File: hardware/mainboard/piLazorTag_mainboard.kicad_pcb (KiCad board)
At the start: 2 copper layers, 10 parts, among them M1 LOGIC_LEVEL_CONVERTER

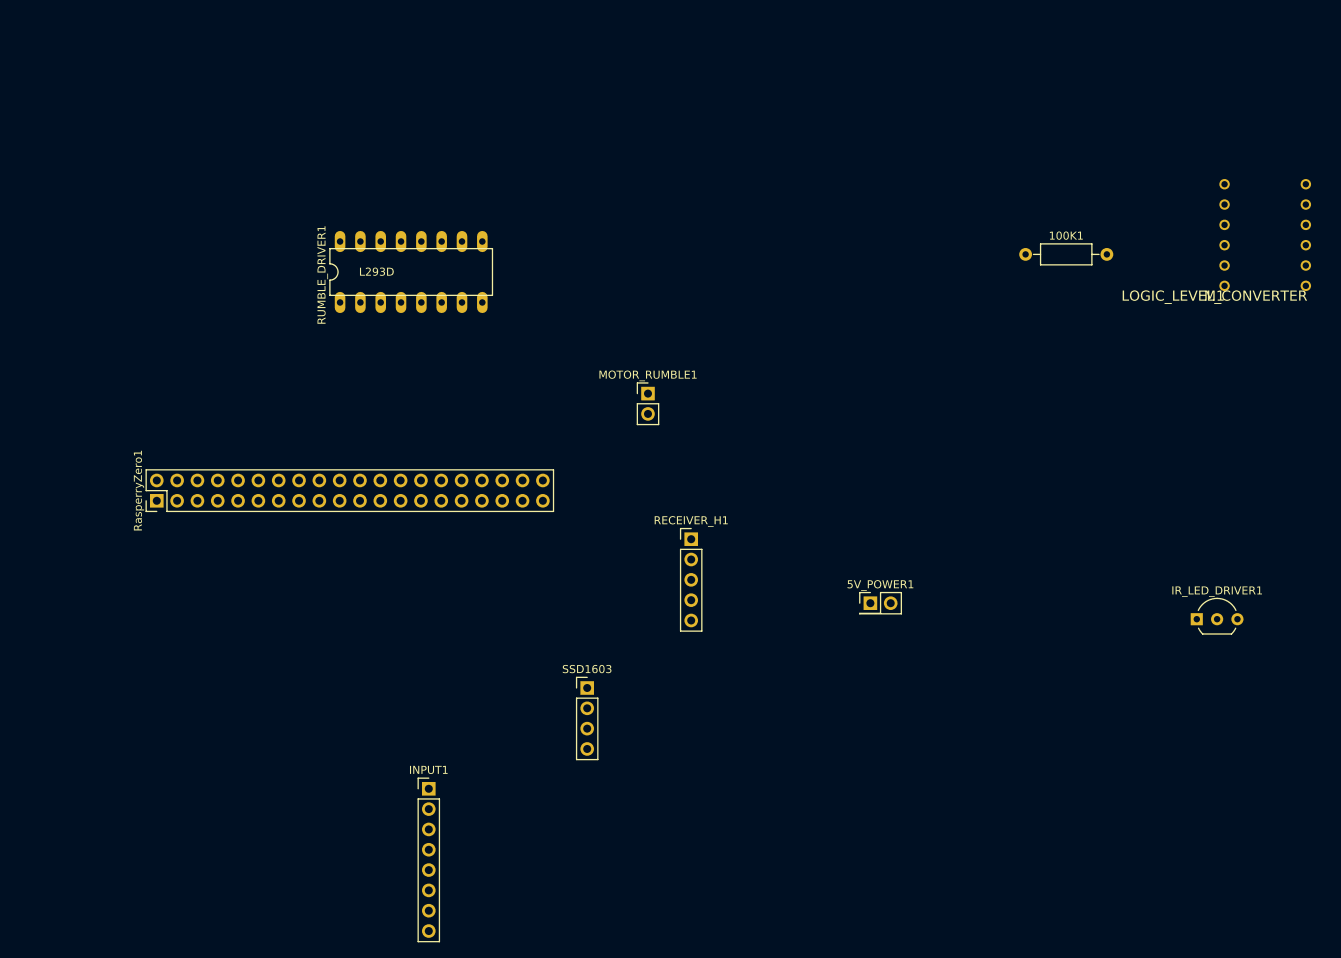
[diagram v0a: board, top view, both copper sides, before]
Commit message: #9 Reasigned some pins to get a better board layout
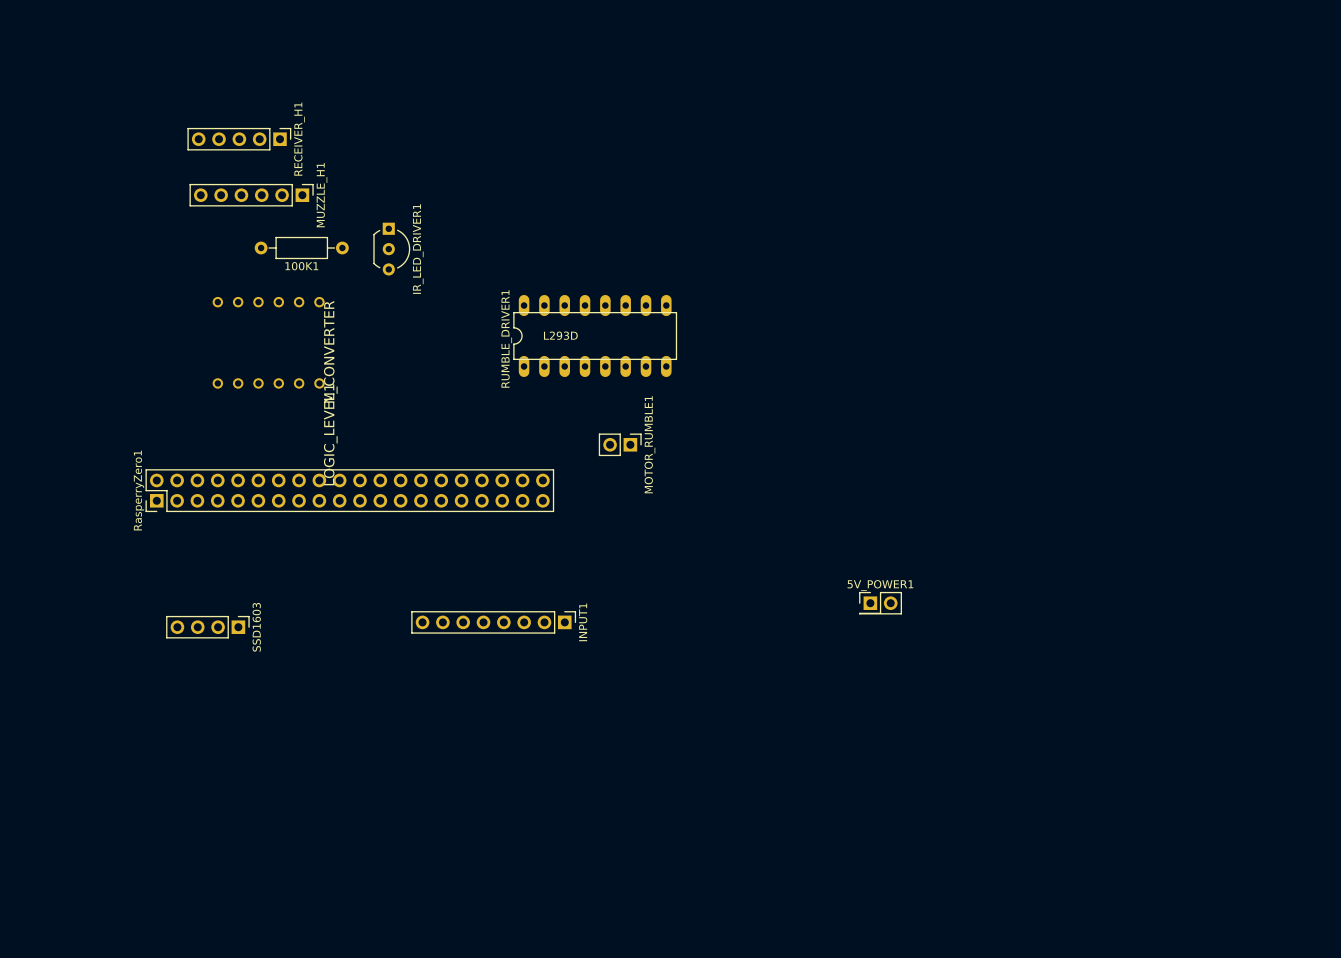
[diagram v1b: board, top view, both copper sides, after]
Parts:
- added MUZZLE_H1: CONN_01X06, Pin_Headers:Pin_Header_Straight_1x06_Pitch2.54mm, F.Cu at (118.0, 74.8)
- moved IR_LED_DRIVER1 112.2 mm to (128.8, 79.0), turned to 270 degrees
- moved M1 111.3 mm to (121.4, 99.6), turned to 90 degrees
- moved 100K1 85.4 mm to (123.0, 81.4), turned to 180 degrees
- moved RECEIVER_H1 71.7 mm to (115.2, 67.8), turned to 270 degrees
- moved SSD1603 44.3 mm to (110.0, 128.8), turned to 270 degrees
- moved INPUT1 26.9 mm to (150.8, 128.2), turned to 270 degrees
- moved RUMBLE_DRIVER1 24.4 mm to (154.6, 92.4)
- moved MOTOR_RUMBLE1 6.77 mm to (159.0, 106.0), turned to 270 degrees
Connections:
- INPUT1 pad 3: Net-(INPUT1-Pad3) -> /G26
- INPUT1 pad 4: Net-(INPUT1-Pad4) -> /G19
- INPUT1 pad 5: Net-(INPUT1-Pad5) -> /G13
- INPUT1 pad 6: Net-(INPUT1-Pad6) -> /G6
- INPUT1 pad 7: Net-(INPUT1-Pad7) -> /G5
- INPUT1 pad 8: Net-(INPUT1-Pad8) -> /G22
- M1 pad P$1: Net-(M1-PadP$1) -> /G18
- M1 pad P$12: Net-(M1-PadP$12) -> /M_LED_DI
- M1 pad P$5: Net-(M1-PadP$5) -> /G23
- M1 pad P$6: Net-(M1-PadP$6) -> /G24
- M1 pad P$7: Net-(M1-PadP$7) -> Net-(100K1-Pad1)
- M1 pad P$8: Net-(M1-PadP$8) -> /IR_SIG
- RUMBLE_DRIVER1 pad 2: /PI_RUMBLE -> /G21

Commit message: #9 Further Progress on the mainboard
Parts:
- moved 5V_POWER1 25.2 mm to (163.8, 125.2), turned to 270 degrees
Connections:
- INPUT1 pad 8: /G22 -> /G11/spi
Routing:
- net +3V3: track 0.00 -> 96.2 mm
- net +5V: track 0.00 -> 29.1 mm
- net /G11/spi: track 0.00 -> 17.6 mm
- net /G3/i2c: track 0.00 -> 15.8 mm
- net /G2/i2c: track 0.00 -> 15.8 mm
- net /G19: track 0.00 -> 15.3 mm
- net /G6: track 0.00 -> 15.3 mm
- net /G5: track 0.00 -> 15.3 mm
- net /G26: track 0.00 -> 15.3 mm
- net /G13: track 0.00 -> 15.3 mm
- net /G21: track 0.00 -> 14.3 mm
- net /G18: track 0.00 -> 14.2 mm
- net Net-(MOTOR_RUMBLE1-Pad2): track 0.00 -> 12.1 mm
- net /G23: track 0.00 -> 12.1 mm
- net /G24: track 0.00 -> 12.1 mm
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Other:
- net class Default: trace_width 0.25 -> 1
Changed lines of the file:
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@@
   (general
     (links 55)
-    (no_connects 55)
+    (no_connects 36)
     (area 0 0 0 0)
     (thickness 1.6)
     (drawings 0)
-    (tracks 0)
+    (tracks 46)
     (zones 0)
     (modules 11)
@@
   )
   (setup
-    (last_trace_width 0.25)
+    (last_trace_width 1)
     (trace_clearance 0.2)
     (zone_clearance 0.508)
@@
   (net_class Default "This is the default net class."
     (clearance 0.2)
-    (trace_width 0.25)
+    (trace_width 1)
     (via_dia 0.6)
     (via_drill 0.4)
@@
   )
   (module Pin_Headers:Pin_Header_Straight_2x01_Pitch2.54mm (layer F.Cu)
-    (at 189 125.8)
+    (at 163.8 125.2 270)
     (descr "Through hole straight pin header, 2x01, 2.54mm pitch, double rows")
     (tags "Through hole pin header THT 2x01 2.54mm double row")
-    (fp_text reference 5V_POWER1 (at 1.27 -2.33) (layer F.SilkS)
-      (effects (font (size 1 1) (thickness 0.15)))
-    )
-    (fp_text value CONN_01X02 (at 1.27 2.33) (layer F.Fab)
+    (fp_text reference 5V_POWER1 (at 1.27 -2.33 270) (layer F.SilkS)
+      (effects (font (size 1 1) (thickness 0.15)))
+    )
+    (fp_text value CONN_01X02 (at 1.27 2.33 270) (layer F.Fab)
       (effects (font (size 1 1) (thickness 0.15)))
     )
@@
     (fp_line (start 4.35 1.8) (end 4.35 -1.8) (layer F.CrtYd) (width 0.05))
     (fp_line (start 4.35 -1.8) (end -1.8 -1.8) (layer F.CrtYd) (width 0.05))
-    (fp_text user %R (at 1.27 -2.33) (layer F.Fab)
-      (effects (font (size 1 1) (thickness 0.15)))
-    )
-    (pad 1 thru_hole rect (at 0 0) (size 1.7 1.7) (drill 1) (layers *.Cu *.Mask)
+    (fp_text user %R (at 1.27 -2.33 270) (layer F.Fab)
+      (effects (font (size 1 1) (thickness 0.15)))
+    )
+    (pad 1 thru_hole rect (at 0 0 270) (size 1.7 1.7) (drill 1) (layers *.Cu *.Mask)
       (net 1 +5V))
-    (pad 2 thru_hole oval (at 2.54 0) (size 1.7 1.7) (drill 1) (layers *.Cu *.Mask)
+    (pad 2 thru_hole oval (at 2.54 0 270) (size 1.7 1.7) (drill 1) (layers *.Cu *.Mask)
       (net 2 GND))
     (model ${KISYS3DMOD}/Pin_Headers.3dshapes/Pin_Header_Straight_2x01_Pitch2.54mm.wrl
@@
       (net 29 /G5))
     (pad 8 thru_hole oval (at 0 17.78 270) (size 1.7 1.7) (drill 1) (layers *.Cu *.Mask)
-      (net 18 /G22))
+      (net 24 /G11/spi))
     (model ${KISYS3DMOD}/Pin_Headers.3dshapes/Pin_Header_Straight_1x08_Pitch2.54mm.wrl
       (at (xyz 0 -0.35 0))
@@
     )
   )
+  (segment (start 163.8 125.2) (end 163.8 96.52) (width 1) (layer B.Cu) (net 1))
+  (segment (start 163.8 96.52) (end 163.49 96.21) (width 1) (layer B.Cu) (net 1))
+  (segment (start 128.66 81.4) (end 128.8 81.54) (width 1) (layer B.Cu) (net 3))
+  (segment (start 145.71 96.21) (end 145.71 88.59) (width 1) (layer B.Cu) (net 6) (status C00000))
+  (segment (start 112.51 98.33) (end 112.51 97.69) (width 1) (layer B.Cu) (net 6) (status C00000))
+  (segment (start 112.51 97.69) (end 113.99 96.21) (width 1) (layer B.Cu) (net 6) (status 400000))
+  (segment (start 113.99 96.21) (end 145.71 96.21) (width 1) (layer B.Cu) (net 6) (status 800000))
+  (segment (start 99.8 113) (end 97.6 113) (width 1) (layer B.Cu) (net 6) (status 400000))
+  (segment (start 109.78 95.6) (end 112.51 98.33) (width 1) (layer B.Cu) (net 6) (status 800000))
+  (segment (start 102.6 95.6) (end 109.78 95.6) (width 1) (layer B.Cu) (net 6))
+  (segment (start 97.2 101) (end 102.6 95.6) (width 1) (layer B.Cu) (net 6))
+  (segment (start 97.2 112.6) (end 97.2 101) (width 1) (layer B.Cu) (net 6))
+  (segment (start 97.6 113) (end 97.2 112.6) (width 1) (layer B.Cu) (net 6))
+  (segment (start 107.46 128.8) (end 107.46 125.66) (width 1) (layer B.Cu) (net 6) (status 400000))
+  (segment (start 107.46 125.66) (end 120.12 113) (width 1) (layer B.Cu) (net 6) (status 800000))
+  (segment (start 159 106) (end 159 96.8) (width 1) (layer B.Cu) (net 8))
+  (segment (start 159 96.8) (end 158.41 96.21) (width 1) (layer B.Cu) (net 8))
+  (segment (start 150.79 96.21) (end 150.79 100.33) (width 1) (layer B.Cu) (net 9))
+  (segment (start 150.79 100.33) (end 156.46 106) (width 1) (layer B.Cu) (net 9))
+  (segment (start 102.38 128.8) (end 102.38 113.04) (width 1) (layer B.Cu) (net 10))
+  (segment (start 102.38 113.04) (end 102.34 113) (width 1) (layer B.Cu) (net 10))
+  (segment (start 104.92 128.8) (end 104.92 113.04) (width 1) (layer B.Cu) (net 11))
+  (segment (start 104.92 113.04) (end 104.88 113) (width 1) (layer B.Cu) (net 11))
+  (segment (start 107.43 98.33) (end 107.43 105.39) (width 1) (layer B.Cu) (net 16))
+  (segment (start 107.43 105.39) (end 112.5 110.46) (width 1) (layer B.Cu) (net 16))
+  (segment (start 117.59 98.33) (end 117.59 110.45) (width 1) (layer B.Cu) (net 19))
+  (segment (start 117.59 110.45) (end 117.58 110.46) (width 1) (layer B.Cu) (net 19))
+  (segment (start 120.13 98.33) (end 120.13 110.45) (width 1) (layer B.Cu) (net 20))
+  (segment (start 120.13 110.45) (end 120.12 110.46) (width 1) (layer B.Cu) (net 20))
+  (segment (start 133.02 128.2) (end 133.02 118.28) (width 1) (layer B.Cu) (net 24) (status 400000))
+  (segment (start 133.02 118.28) (end 127.74 113) (width 1) (layer B.Cu) (net 24) (status 800000))
+  (segment (start 133.02 128.2) (end 132.78 128.2) (width 1) (layer B.Cu) (net 24))
+  (segment (start 135.56 128.2) (end 135.56 113.2) (width 1) (layer B.Cu) (net 29))
+  (segment (start 135.56 113.2) (end 135.36 113) (width 1) (layer B.Cu) (net 29))
+  (segment (start 137.9 113) (end 137.9 128) (width 1) (layer B.Cu) (net 30))
+  (segment (start 137.9 128) (end 138.1 128.2) (width 1) (layer B.Cu) (net 30))
+  (segment (start 140.64 128.2) (end 140.64 113.2) (width 1) (layer B.Cu) (net 32))
+  (segment (start 140.64 113.2) (end 140.44 113) (width 1) (layer B.Cu) (net 32))
+  (segment (start 142.98 113) (end 142.98 128) (width 1) (layer B.Cu) (net 33))
+  (segment (start 142.98 128) (end 143.18 128.2) (width 1) (layer B.Cu) (net 33))
+  (segment (start 145.72 128.2) (end 145.72 113.2) (width 1) (layer B.Cu) (net 35))
+  (segment (start 145.72 113.2) (end 145.52 113) (width 1) (layer B.Cu) (net 35))
+  (segment (start 148.06 110.46) (end 148.06 96.4) (width 1) (layer B.Cu) (net 37))
+  (segment (start 148.06 96.4) (end 148.25 96.21) (width 1) (layer B.Cu) (net 37))
+  (segment (start 105.3 68.06) (end 105.04 67.8) (width 1) (layer B.Cu) (net 39))
+  (segment (start 107.43 75.21) (end 107.84 74.8) (width 1) (layer B.Cu) (net 45))
 )
